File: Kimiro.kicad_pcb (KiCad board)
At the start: 2 copper layers, 17.8 x 33 mm, 26 parts, among them J2 USB_C_Left, J3 Left, J4 Right, Q1 AO3407, U2 TP4054, U3 MS88FS3, U4 XC6220B331MR

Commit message: Kicad PCB design ver 1.1
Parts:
- removed C8: 0.1uF, Capacitor_SMD:C_0402_1005Metric
- removed D3: RED, LED_SMD:LED_0603_1608Metric
- removed J4: Right, Sakura-library:Conn_1x13_P2.54mm
- removed Q1: AO3407, Package_TO_SOT_SMD:SOT-23
- removed R11: 1K, Resistor_SMD:R_0402_1005Metric
- added C2: 4.7uF, Capacitor_SMD:C_0402_1005Metric, F.Cu at (78.6, 46.7)
- added C3: 4.7uF, Capacitor_SMD:C_0402_1005Metric, F.Cu at (70.7, 41.3)
- added C4: 10uF, Capacitor_SMD:C_0402_1005Metric, F.Cu at (79.3, 42.3)
- added J1: USB_C_Left, footprints:USB-C_C168688, F.Cu at (76.2, 32.5)
- added R6: 10k, Resistor_SMD:R_0402_1005Metric, F.Cu at (70.8, 42.3)
- added R7: 820K, Resistor_SMD:R_0402_1005Metric, F.Cu at (72.8, 41.3)
- added TP1: TestPoint, TestPoint:TestPoint_Pad_1.5x1.5mm, B.Cu at (74.3, 52.4)
- added TP10: TestPoint, TestPoint:TestPoint_Pad_1.5x1.5mm, B.Cu at (77.3, 54.9)
- added TP2: TestPoint, TestPoint:TestPoint_Pad_1.5x1.5mm, B.Cu at (74.3, 57.3)
- added TP3: TestPoint, TestPoint:TestPoint_Pad_1.5x1.5mm, B.Cu at (74.3, 54.8)
- added TP4: TestPoint, TestPoint:TestPoint_Pad_1.5x1.5mm, B.Cu at (74.3, 50.0)
- added TP5: TestPoint, TestPoint:TestPoint_Pad_1.5x1.5mm, B.Cu at (74.3, 59.7)
- added TP6: TestPoint, TestPoint:TestPoint_Pad_1.5x1.5mm, B.Cu at (77.3, 52.5)
- added TP7: TestPoint, TestPoint:TestPoint_Pad_1.5x1.5mm, B.Cu at (77.3, 57.3)
- added TP8: TestPoint, TestPoint:TestPoint_Pad_1.5x1.5mm, B.Cu at (77.3, 59.7)
- added TP9: TestPoint, TestPoint:TestPoint_Pad_1.5x1.5mm, B.Cu at (77.3, 50.0)
- added kibuzzard-62308F3A: G***, kibuzzard-62308F3A, B.Cu at (75.6, 47.8)
- added kibuzzard-62308F5E: G***, kibuzzard-62308F5E, B.Cu at (79.7, 47.8)
- added kibuzzard-6230908B: G***, kibuzzard-6230908B, B.Cu at (76.3, 63.5)
- added kibuzzard-623091BE: G***, kibuzzard-623091BE, F.Cu at (76.3, 63.5)
- C1: value 10uF -> 1uF
- C5: value 10uF -> 4.7uF
- C6: value 4.7uF -> 0.1uF
- D1: value 1N5819 -> RED; footprint Diode_SMD:D_SOD-323F -> LED_SMD:LED_0603_1608Metric
- J2: value USB_C_Left -> Left; footprint kien242:USB-C-Low -> Kimiro-library:Conn_1x13_P2.54mm
- J3: value Left -> Right; footprint Sakura-library:Conn_1x13_P2.54mm -> Kimiro-library:Conn_1x13_P2.54mm
- R10: value 10K -> 1K
- R3: value 100K -> 10k
- R4: value 1K -> 10k
- R5: value RPROG -> 3.9k
- R8: value 820K -> 2M
- R9: value 2M -> 10K
- U1: renamed from U2; value TP4054 -> BQ24075RGT; footprint Package_TO_SOT_SMD:SOT-23-5 -> Package_DFN_QFN:VQFN-16-1EP_3x3mm_P0.5mm_EP1.6x1.6mm
- moved SWD1 39.9 mm to (79.7, 55.1), turned to 90 degrees
- moved J3 15.2 mm to (83.8, 34.3)
- moved D2 11.2 mm to (81.9, 44.4)
- moved J2 8.76 mm to (68.6, 34.3)
- moved C5 7.99 mm to (81.4, 42.3), turned to 0 degrees
- moved R10 7.76 mm to (81.4, 41.3), turned to 0 degrees
- moved U1 6.98 mm to (73.8, 43.9), turned to -90 degrees
- moved C1 6.00 mm to (81.3, 40.3), turned to 0 degrees
- moved D1 5.99 mm to (70.7, 44.4), turned to 90 degrees
- moved R9 5.82 mm to (80.8, 46.7), turned to 0 degrees
- moved R3 5.77 mm to (77.1, 41.3), turned to 0 degrees
- moved R4 4.62 mm to (76.4, 44.4)
- moved R5 4.08 mm to (77.1, 42.3), turned to 0 degrees
- moved C6 3.54 mm to (76.3, 46.7), turned to 180 degrees
- moved R8 3.27 mm to (75.0, 41.3), turned to 0 degrees
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- renumbered U3 to U2, U4 to U3
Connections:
- net LED renamed BLUE_LED
- C1 pad 1: GND -> VBUS
- C1 pad 2: VBUS -> GND
- C5 pad 2: VDDH -> VCC
- C6 pad 1: GND -> VDDH
- C6 pad 2: VCC -> GND
- D1 pad 1: VDDH -> Net-(D1-Pad1)
- D1 pad 2: VBUS -> Net-(D1-Pad2)
- J3 pad 1: GND -> VBAT
- J3 pad 10: unconnected-(J3-Pad10) -> P0.27
- J3 pad 11: unconnected-(J3-Pad11) -> P0.26
- J3 pad 12: unconnected-(J3-Pad12) -> P0.07
- J3 pad 13: unconnected-(J3-Pad13) -> P0.06
- J3 pad 2: unconnected-(J3-Pad2) -> VBAT
- J3 pad 3: unconnected-(J3-Pad3) -> GND
- J3 pad 4: GND -> RST
- J3 pad 5: GND -> VCC
- J3 pad 6: unconnected-(J3-Pad6) -> P0.05
- J3 pad 7: unconnected-(J3-Pad7) -> P0.04
- J3 pad 8: unconnected-(J3-Pad8) -> P0.03
- J3 pad 9: unconnected-(J3-Pad9) -> P0.02
- R1 pad 1: Net-(J2-PadA5) -> Net-(J1-PadA5)
- R10 pad 1: VDDH -> GND
- R10 pad 2: POWER_PIN -> Net-(D2-Pad1)
- R2 pad 2: Net-(J2-PadB5) -> Net-(J1-PadB5)
- R3 pad 1: VBUS -> Net-(R3-Pad1)
- R4 pad 1: Net-(D3-Pad1) -> CHARGE_CTRL_1
- R5 pad 1: Net-(R5-Pad1) -> Net-(R4-Pad2)
- R5 pad 2: GND -> CHARGE_CTRL_2
- R8 pad 1: VBAT -> BATTERY_PIN
- R8 pad 2: BATTERY_PIN -> GND
- R9 pad 1: BATTERY_PIN -> VDDH
- R9 pad 2: GND -> POWER_PIN
- U1 pad 1: Net-(R4-Pad2) -> Net-(R3-Pad1)
- U1 pad 2: GND -> VBAT
- U1 pad 4: VBUS -> GND
- U1 pad 5: Net-(R5-Pad1) -> GND
- U2 pad 10: unconnected-(U3-Pad10) -> P0.29
- U2 pad 11: unconnected-(U3-Pad11) -> BATTERY_PIN
- U2 pad 12: unconnected-(U3-Pad12) -> P0.30
- U2 pad 13: unconnected-(U3-Pad13) -> P0.31
- U2 pad 14: unconnected-(U3-Pad14) -> P0.27
- U2 pad 15: unconnected-(U3-Pad15) -> P0.05
- U2 pad 16: unconnected-(U3-Pad16) -> P0.04
- U2 pad 17: unconnected-(U3-Pad17) -> P0.26
- U2 pad 19: unconnected-(U3-Pad19) -> P0.07
- U2 pad 2: unconnected-(U3-Pad2) -> P1.11
- U2 pad 20: unconnected-(U3-Pad20) -> P0.06
- U2 pad 21: unconnected-(U3-Pad21) -> P1.08
- U2 pad 22: unconnected-(U3-Pad22) -> P0.11
- U2 pad 25: unconnected-(U3-Pad25) -> P0.08
- U2 pad 26: unconnected-(U3-Pad26) -> P1.09
- U2 pad 27: unconnected-(U3-Pad27) -> P0.12
- U2 pad 3: unconnected-(U3-Pad3) -> P1.12
- U2 pad 34: unconnected-(U3-Pad34) -> GND
- U2 pad 38: unconnected-(U3-Pad38) -> P0.19
- U2 pad 39: unconnected-(U3-Pad39) -> P0.13
- U2 pad 4: unconnected-(U3-Pad4) -> P1.10
- U2 pad 40: unconnected-(U3-Pad40) -> P0.15
- U2 pad 41: unconnected-(U3-Pad41) -> P0.17
- U2 pad 42: unconnected-(U3-Pad42) -> P0.21
- U2 pad 43: unconnected-(U3-Pad43) -> P0.23
- U2 pad 44: unconnected-(U3-Pad44) -> P0.20
- U2 pad 45: unconnected-(U3-Pad45) -> P0.22
- U2 pad 46: unconnected-(U3-Pad46) -> P0.24
- U2 pad 47: unconnected-(U3-Pad47) -> P1.00
- U2 pad 48: unconnected-(U3-Pad48) -> P0.25
- U2 pad 5: unconnected-(U3-Pad5) -> P1.14
- U2 pad 6: unconnected-(U3-Pad6) -> P0.03
- U2 pad 7: unconnected-(U3-Pad7) -> P1.13
- U2 pad 8: unconnected-(U3-Pad8) -> P1.15
- U2 pad 9: unconnected-(U3-Pad9) -> P0.02
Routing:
- net GND: track 36.4 -> 118.7 mm, vias 0 -> 21
- net VDDH: track 4.60 -> 36.4 mm, vias 0 -> 4
- net BATTERY_PIN: track 0.99 -> 27.7 mm, vias 0 -> 3
- net VBAT: track 1.36 -> 26.3 mm, vias 0 -> 1
- net P0.19: track 0.00 -> 18.4 mm, vias 0 -> 1
- net P0.06: track 0.00 -> 18.3 mm, vias 0 -> 1
- net D+: track 0.00 -> 17.7 mm, vias 0 -> 2
- net P0.13: track 0.00 -> 16.4 mm, vias 0 -> 1
- net D-: track 0.00 -> 16.4 mm, vias 0 -> 3
- net P0.07: track 0.00 -> 15.6 mm, vias 0 -> 1
- net P0.11: track 0.00 -> 15.0 mm, vias 0 -> 3
- net P1.08: track 0.00 -> 14.0 mm, vias 0 -> 3
- net RST: track 0.00 -> 13.3 mm, vias 0 -> 1
- net VDD: track 1.31 -> 14.1 mm
- net SWDIO: track 0.00 -> 12.8 mm, vias 0 -> 1
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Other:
- board text added: "+"
- board text added: "-"
- board text added: "002"
- board text added: "003"
- board text added: "004"
- board text added: "005"
- board text added: "006"
- board text added: "007"
- board text added: "008"
- board text added: "011"
- board text added: "012"
- board text added: "013"
- board text added: "015"
- board text added: "017"
- board text added: "019"
- board text added: "020"
- board text added: "021"
- board text added: "022"
- board text added: "023"
- board text added: "024"
- board text added: "026"
- board text added: "027"
- board text added: "030"
- board text added: "031"
- board text added: "100"
- board text added: "108"
- board text added: "109"
- board text added: "113"
- board text added: "114"
- board text added: "115"
- board text added: "3.3V"
- board text added: "CLK"
- board text added: "DIO"
- board text added: "Design by kien242 & deemen17"
- board text added: "GND"
- board text added: "RST"
- board text added: "VBAT"
- board text added: "VCC"

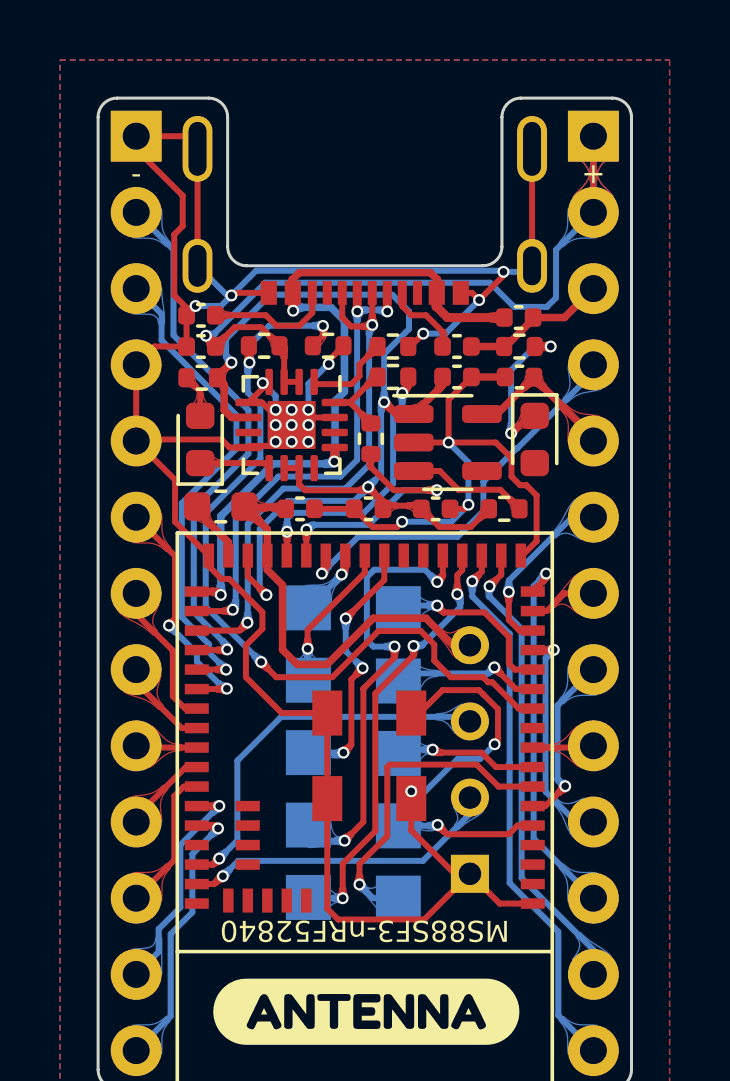
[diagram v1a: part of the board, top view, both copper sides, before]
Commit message: Fix VBUS trace nears USB edge-cut
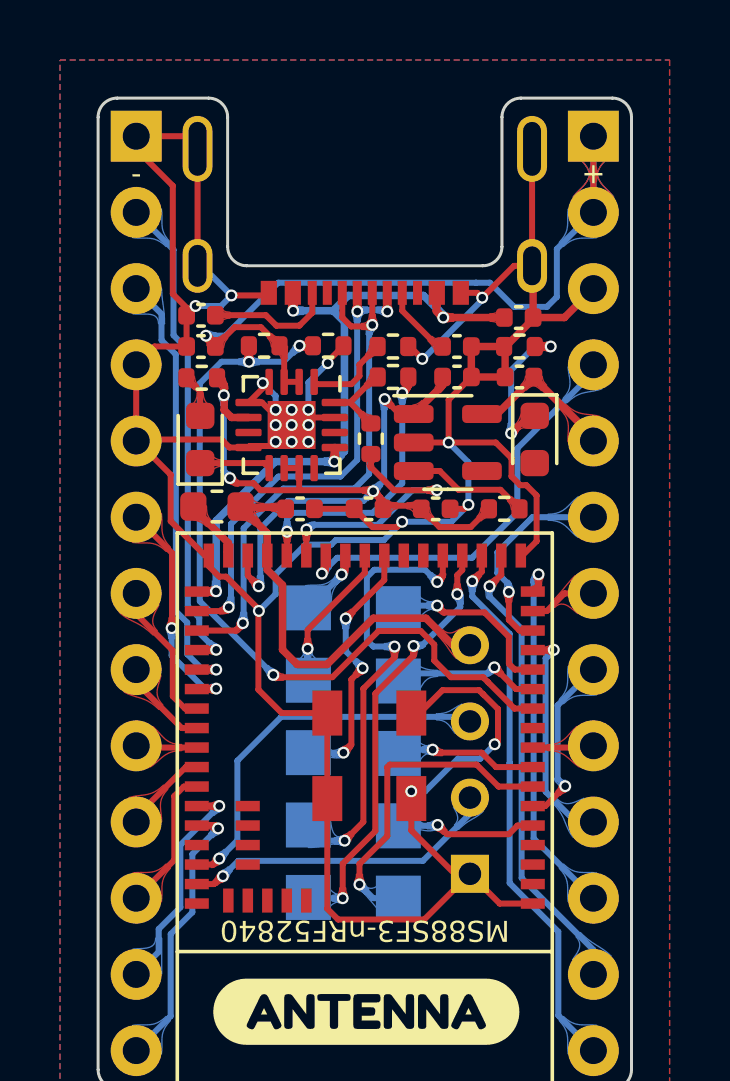
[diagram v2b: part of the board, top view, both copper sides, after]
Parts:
- moved L1 0.13 mm to (71.3, 46.6)
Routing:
- net VDDH: track 36.4 -> 29.4 mm, vias 4 -> 5
- net P0.19: track 18.4 -> 16.3 mm
- net VBUS: track 24.6 -> 22.8 mm, vias 3 -> 4
- net P0.13: track 16.4 -> 14.7 mm
- net BATTERY_PIN: track 27.7 -> 26.3 mm
- net P0.05: track 5.95 -> 7.04 mm
- net GND: track 118.7 -> 119.8 mm
- net RST: track 13.3 -> 14.0 mm

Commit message: Remove some needless via
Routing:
- net GND: track 119.8 -> 112.5 mm, vias 21 -> 18

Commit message: Check again and add note slikscreen for extra pins
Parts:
- moved kibuzzard-62308F3A 0.05 mm to (75.6, 47.8)
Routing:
- net GND: track 112.5 -> 111.8 mm
- net P1.09: track 5.43 -> 4.92 mm
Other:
- board text added: "HIGH"
- board text added: "LOW"
